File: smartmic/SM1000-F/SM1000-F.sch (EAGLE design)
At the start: 205 parts, among them CN1 HDR100-3, CN10 ST-3509, CN11 HDR100-3, CN12 HRS-A3C-16DA, CN2 JS-MU3-002, CN3 DS-0518, CN4 RJ-45, CN5 ST-3509, CN6 ST-3509, CN7 ST-3509, CN8 ST-3509, CN9 ST-3509, J1 JMP-2PIN, J2 JMP-2PIN, J3 JMP-2PIN, J4 CONN-BOOM-XH-2A, P1 TPAD50, P10 TPAD50, P11 TPAD50, P12 TPAD50, P13 TPAD50, P14 TPAD50, P16 TPAD50, P18 TPAD50, P19 TPAD50, P2 TPAD50, P20 TPAD50, P3 TPAD50, P4 TPAD50, P5 TPAD50, P6 TPAD50, P7 TPAD50, P8 TPAD50, P9 TPAD50, SW1 SW-LC2259, SW2 TS-026, SW3 SW-LC2259EENP, SW4 TS-026, SW5 TS-02B, T1 SM-LP-5001, T2 SM-LP-5001, U1 STM32F405VGT6, U2 LD3985M33R, U3 STMPS2141, U4 EMIF02-USB03F2, U5 TPS54329E, U6 LMV341, U7 LMV341, U8 LM386M-1, U9 LMV341

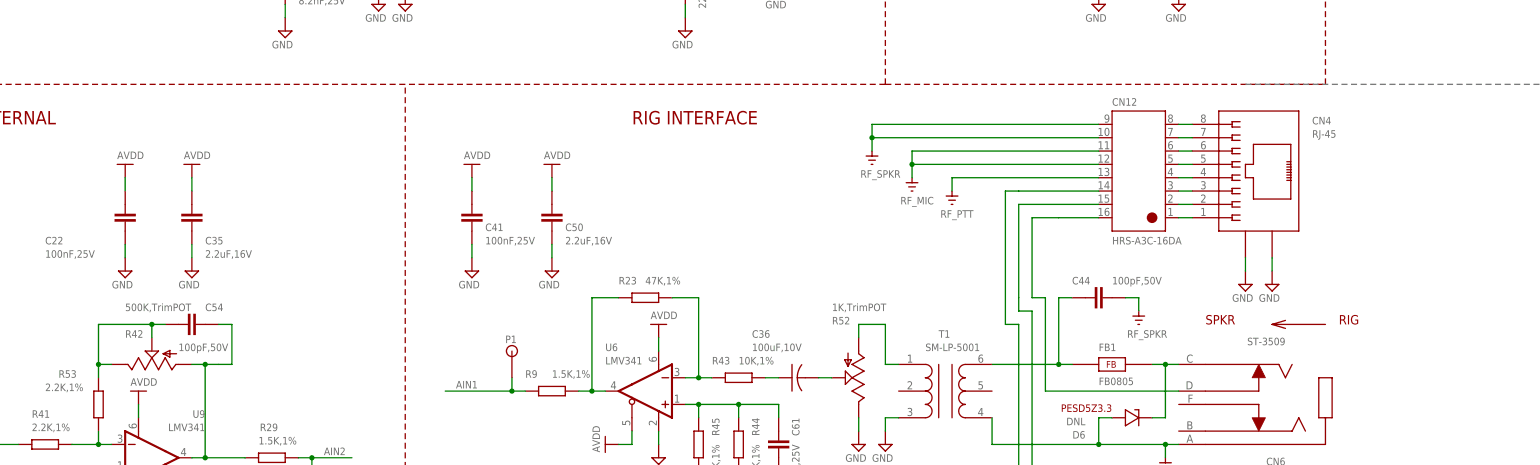
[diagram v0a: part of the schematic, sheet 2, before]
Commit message: Started implementing change-log items 34-41 RGB 09/15/15
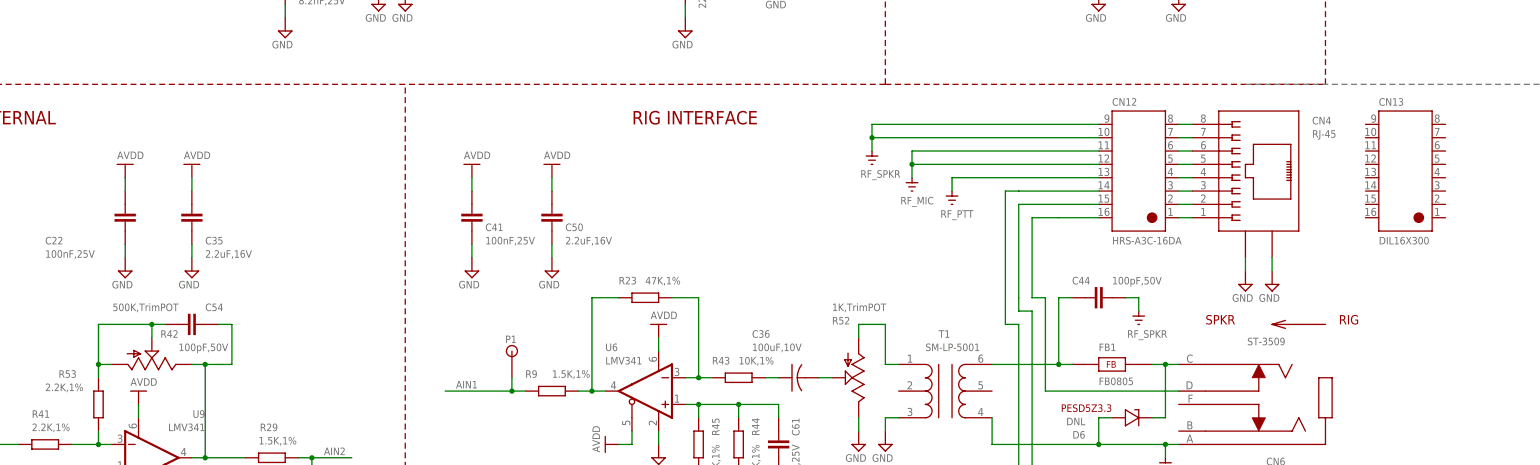
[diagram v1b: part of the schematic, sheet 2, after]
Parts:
- added CN13: DIL16X300, _RoweTel:DIL16X300
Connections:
- net N$27: now also R42.1; no longer R42.3
- net N$41: now also R42.3; no longer R42.1
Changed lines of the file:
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@@
 <part name="V143" library="A-SUPPLY2" deviceset="GND" device=""/>
 <part name="D8" library="_RoweTel" deviceset="PESD5ZX" device="" value="DNL"/>
+<part name="CN13" library="_RoweTel" deviceset="DIL16X300" device=""/>
 </parts>
 <sheets>
@@
 <attribute name="VALUE" x="106.68" y="134.62" size="1.4224" layer="96" ratio="9"/>
 </instance>
-<instance part="R42" gate="G$1" x="129.54" y="147.32" smashed="yes" rot="R90">
-<attribute name="NAME" x="124.46" y="152.4" size="1.4224" layer="95" ratio="9"/>
-<attribute name="VALUE" x="124.46" y="157.48" size="1.4224" layer="96" ratio="9"/>
+<instance part="R42" gate="G$1" x="129.54" y="147.32" smashed="yes" rot="MR90">
+<attribute name="NAME" x="134.62" y="152.4" size="1.4224" layer="95" ratio="9" rot="MR0"/>
+<attribute name="VALUE" x="134.62" y="157.48" size="1.4224" layer="96" ratio="9" rot="MR0"/>
 </instance>
 <instance part="V62" gate="GND" x="111.76" y="109.22" smashed="yes">
@@
 <attribute name="VALUE" x="45.72" y="119.38" size="1.4224" layer="96" ratio="10"/>
 </instance>
+<instance part="CN13" gate="G$1" x="368.3" y="182.88" smashed="yes">
+<attribute name="NAME" x="363.22" y="196.596" size="1.4224" layer="95" ratio="10"/>
+<attribute name="VALUE" x="363.22" y="170.18" size="1.4224" layer="96" ratio="10"/>
+</instance>
 </instances>
 <busses>
@@
 <net name="N$41" class="0">
 <segment>
-<wire x1="119.38" y1="147.32" x2="121.92" y2="147.32" width="0.1524" layer="91"/>
-<pinref part="R42" gate="G$1" pin="1"/>
-<pinref part="R42" gate="G$1" pin="2"/>
-<wire x1="129.54" y1="152.4" x2="129.54" y2="154.94" width="0.1524" layer="91"/>
 <wire x1="129.54" y1="154.94" x2="119.38" y2="154.94" width="0.1524" layer="91"/>
 <wire x1="119.38" y1="154.94" x2="119.38" y2="147.32" width="0.1524" layer="91"/>
 <pinref part="R53" gate="G$1" pin="2"/>
 <wire x1="119.38" y1="144.78" x2="119.38" y2="147.32" width="0.1524" layer="91"/>
-<junction x="119.38" y="147.32"/>
 <wire x1="129.54" y1="154.94" x2="132.08" y2="154.94" width="0.1524" layer="91"/>
-<junction x="129.54" y="154.94"/>
 <pinref part="C54" gate="G$1" pin="1"/>
+<pinref part="R42" gate="G$1" pin="3"/>
+<wire x1="121.92" y1="147.32" x2="119.38" y2="147.32" width="0.1524" layer="91"/>
+<pinref part="R42" gate="G$1" pin="2"/>
+<wire x1="129.54" y1="152.4" x2="129.54" y2="154.94" width="0.1524" layer="91"/>
+<junction x="129.54" y="154.94"/>
+<junction x="119.38" y="147.32"/>
 </segment>
 </net>
@@
 <net name="N$27" class="0">
 <segment>
-<pinref part="R42" gate="G$1" pin="3"/>
-<wire x1="137.16" y1="147.32" x2="139.7" y2="147.32" width="0.1524" layer="91"/>
 <pinref part="U9" gate="G$1" pin="OUT"/>
 <pinref part="R29" gate="G$1" pin="2"/>
@@
 <wire x1="139.7" y1="147.32" x2="139.7" y2="129.54" width="0.1524" layer="91"/>
 <junction x="139.7" y="129.54"/>
-<junction x="139.7" y="147.32"/>
 <pinref part="C54" gate="G$1" pin="2"/>
 <wire x1="142.24" y1="154.94" x2="144.78" y2="154.94" width="0.1524" layer="91"/>
 <wire x1="144.78" y1="154.94" x2="144.78" y2="147.32" width="0.1524" layer="91"/>
 <wire x1="144.78" y1="147.32" x2="142.24" y2="147.32" width="0.1524" layer="91"/>
+<pinref part="R42" gate="G$1" pin="1"/>
+<wire x1="137.16" y1="147.32" x2="139.7" y2="147.32" width="0.1524" layer="91"/>
+<junction x="139.7" y="147.32"/>
 </segment>
 </net>

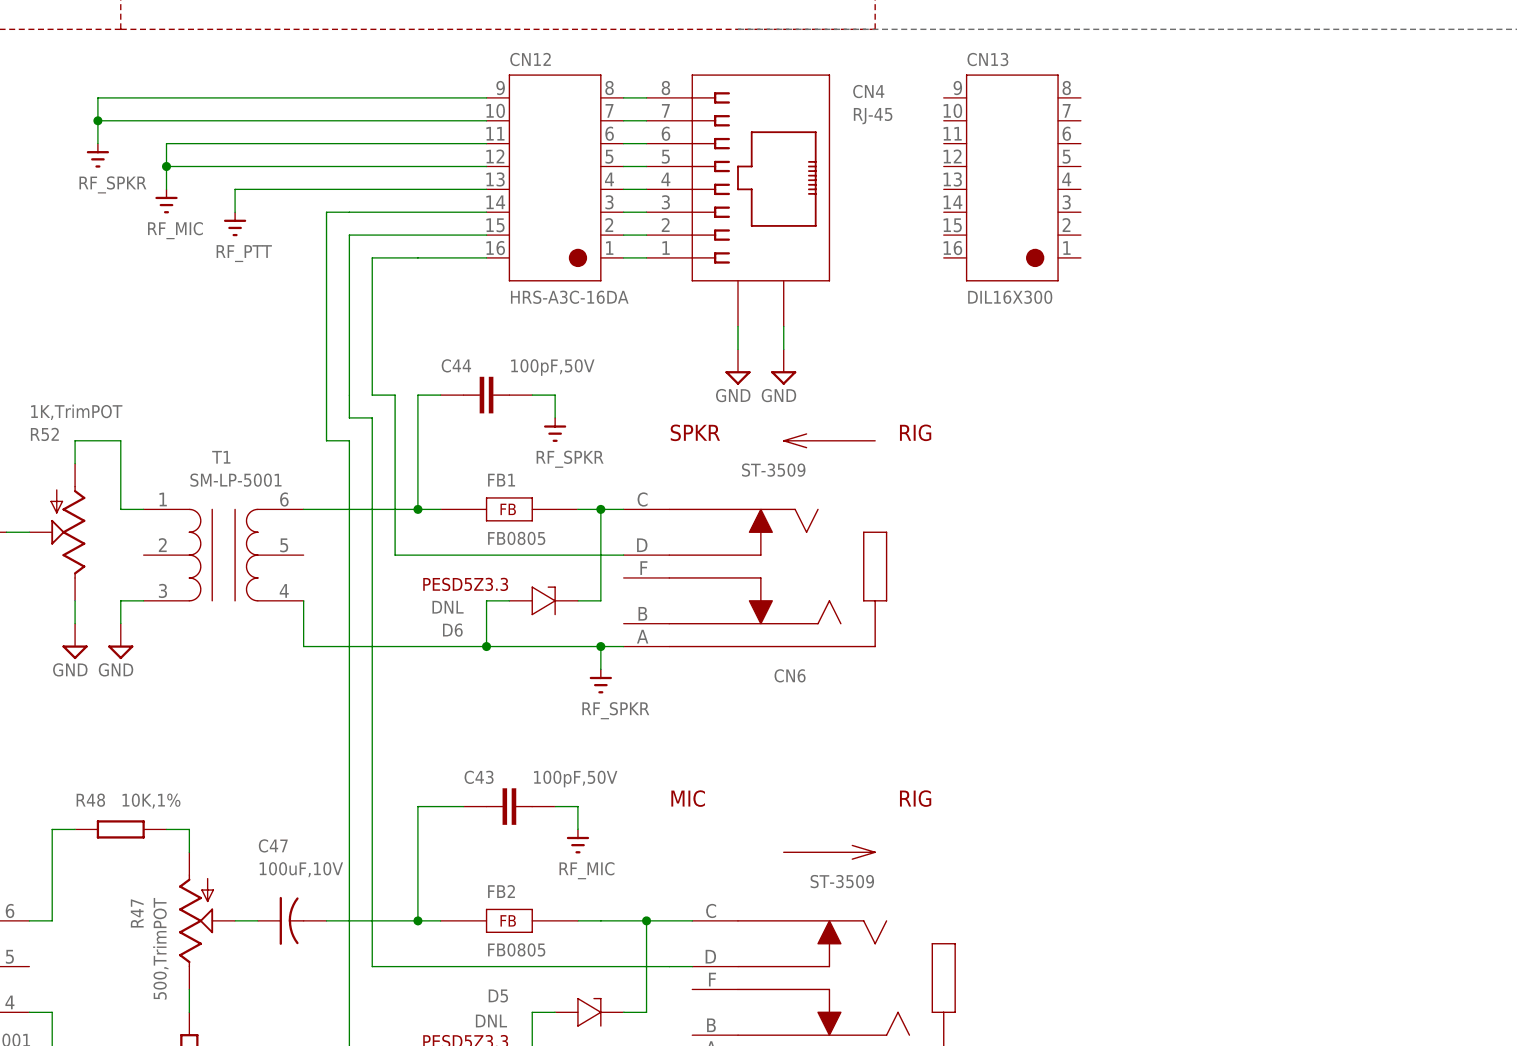
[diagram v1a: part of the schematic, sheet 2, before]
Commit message: Show Schematic changes for CN12 pin swaps.  RGB 09/16/15
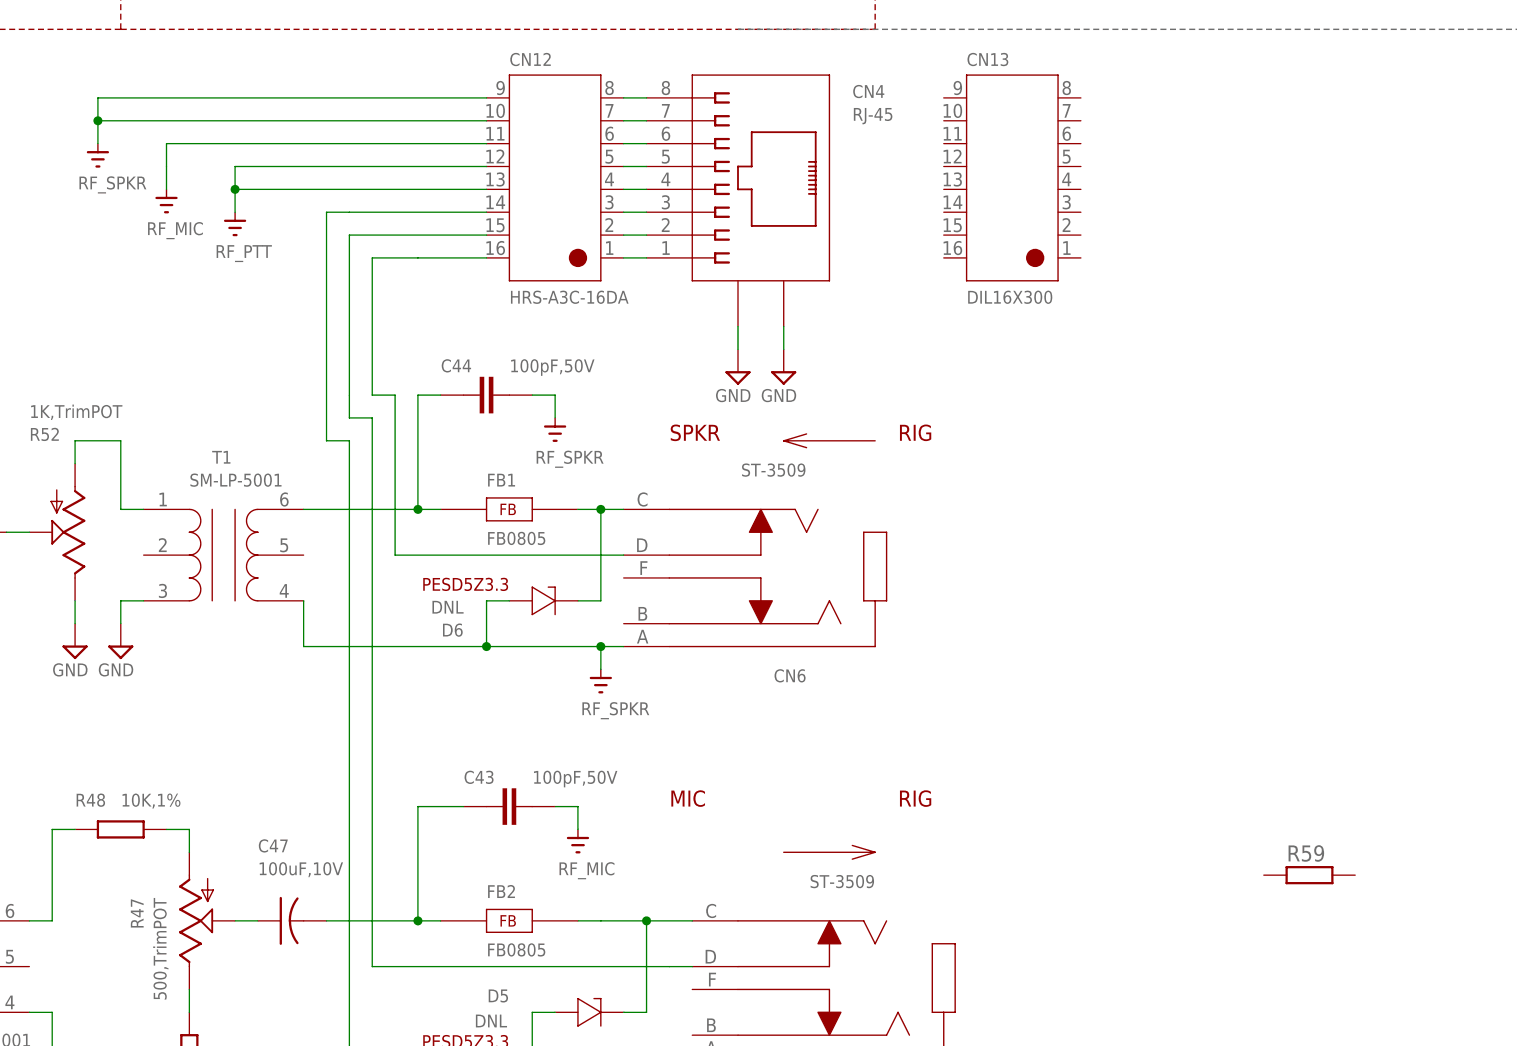
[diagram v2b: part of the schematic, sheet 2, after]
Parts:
- added R59: (no value), AA-ipc-7351-resistor:RESISTOR_1206
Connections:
- net RF_MIC: no longer CN12.12
- net RF_PTT: now also CN12.12
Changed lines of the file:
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@@
 <part name="D8" library="_RoweTel" deviceset="PESD5ZX" device="" value="DNL"/>
 <part name="CN13" library="_RoweTel" deviceset="DIL16X300" device=""/>
+<part name="R59" library="AA-ipc-7351-resistor" deviceset="RESISTOR_" device="1206"/>
 </parts>
 <sheets>
@@
 <attribute name="VALUE" x="363.22" y="170.18" size="1.4224" layer="96" ratio="10"/>
 </instance>
+<instance part="R59" gate="G$1" x="401.32" y="106.68"/>
 </instances>
 <busses>
@@
 <wire x1="274.32" y1="187.96" x2="274.32" y2="185.42" width="0.1524" layer="91"/>
 <wire x1="274.32" y1="185.42" x2="274.32" y2="182.88" width="0.1524" layer="91"/>
-<wire x1="309.88" y1="185.42" x2="274.32" y2="185.42" width="0.1524" layer="91"/>
-<junction x="274.32" y="185.42"/>
 <pinref part="V133" gate="G$1" pin="RF_MIC"/>
 <pinref part="CN12" gate="G$1" pin="11"/>
-<pinref part="CN12" gate="G$1" pin="12"/>
 </segment>
 <segment>
@@
 <pinref part="V92" gate="G$1" pin="RF_PTT"/>
 <pinref part="CN12" gate="G$1" pin="13"/>
+<pinref part="CN12" gate="G$1" pin="12"/>
+<wire x1="309.88" y1="185.42" x2="281.94" y2="185.42" width="0.1524" layer="91"/>
+<wire x1="281.94" y1="185.42" x2="281.94" y2="182.88" width="0.1524" layer="91"/>
+<junction x="281.94" y="182.88"/>
 </segment>
 </net>

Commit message: Update Schematic & board files. Add PDF of schematic for review. RGB
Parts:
- removed CN12: HRS-A3C-16DA, _RoweTel:HRS-A3C-16DA
- removed CN13: DIL16X300, _RoweTel:DIL16X300
- added CN112: DIL16X300, _RoweTel:DIL16X300
- added J5: JMP-2PIN, _Coherix:JMP-2PIN
- added P15, P17, P21: TPAD50, _Coherix:TPAD50
- added R60: 330,1%, AA-ipc-7351-resistor:RESISTOR_1206
- added R61, R62: (no value), AA-ipc-7351-resistor:RESISTOR_0603
- added SH4: SHUNT,0.1IN, _Coherix:SHUNT,0.1IN
- added U10: 24LC256-I/MS, coherix:I2C-EEPROM-256KMSOP-8
- R48: device AA-ipc-7351-resistor:RESISTOR_0402 -> AA-ipc-7351-resistor:RESISTOR_1206
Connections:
- new net N$75: J5.2, R60.1
- new net SCL3: R62.2, U10.SCL, U1A.PE10
- new net SDA3: R61.2, U10.SDA, U1A.PE9
- net APTT: now also CN112.14; no longer CN12.14
- net GND: now also P17.1, U10.A0, U10.A1, U10.A2, U10.GND, U10.WP
- net MIC: now also CN112.15; no longer CN12.15
- net N$51: now also CN112.8, P15.1; no longer CN12.8
- net N$52: now also CN112.7; no longer CN12.7
- net N$53: now also CN112.6; no longer CN12.6
- net N$54: now also CN112.5; no longer CN12.5
- net N$55: now also CN112.4; no longer CN12.4
- net N$56: now also CN112.3; no longer CN12.3
- net N$57: now also CN112.2; no longer CN12.2
- net N$58: now also CN112.1; no longer CN12.1
- net N$77: now also P21.1
- net N$78: now also R60.2
- net N$82: now also J5.1
- net RF_MIC: now also CN112.11; no longer CN12.11
- net RF_PTT: now also CN112.12, CN112.13; no longer CN12.12, CN12.13
- net RF_SPKR: now also CN112.10, CN112.9; no longer CN12.10, CN12.9
- net SPKR: now also CN112.P16; no longer CN12.P16
- net VDD: now also R61.1, R62.1, U10.VCC
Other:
- note added: "09/27/15"
- note added: "ADD EEPROM FOR PERSISTANT MEMORY."
- note added: "ADD EEPROM FOR PERSISTENT MEMORY."
- note added: "ADD PADS FOR USING RIG POWER."
- note added: "ADD R& JMPR IN PARALLEL WITH R48."
- note added: "ADDR: 0XA0"
- note added: "CHANGE GROUNDING ON CN13."
- note added: "CHANGE R48 & R60 FOR USER CHANGE."
- note added: "CN12 -> .3" DIL FOR EASIER CONFIG."
- note added: "EEPROM"
- note added: "POTS FISED FOR CW ROTATION."
- note added: "Rev E. -> Rev F CHANGES"
- note removed: "01-23-15"
- note removed: "01/13/15"
- note removed: "01/14/15"
- note removed: "01/23/15"
- note removed: "05/19/15"
- note removed: "05/20/15"
- note removed: "05/27/15"
- note removed: "06/01/15"
- note removed: "06/05/15"
- note removed: "06/26/15"
- note removed: "06/27/15"
- note removed: "11/23/14"
- note removed: "ADD D1,D3,D4,D5,D6,D7,D8 TSV"
- note removed: "ADD MISC. PARTS TO BOM"
- note removed: "CHANGE CIRCUITRY FOR CN8"
- note removed: "CHANGE CIRCUITRY TO FIX CN8 PROBLEM"
- note removed: "CHANGE LED COLORS FOR LED1 , LED4"
- note removed: "CHANGE PARTS SW1, SW3 & J4"
- note removed: "CHANGE R42,R47 & R52 TO TYPE 3361"
- note removed: "Change SW1 to MULTICOMP SPDT"
- note removed: "D"
- note removed: "DNL LED5,R17,LED8,R33"
- note removed: "E"
- note removed: "FIX TS-026 FOOTPRINT"
- note removed: "MOVE SW3,4 TO EDGE"
- note removed: "MOVE USB CONN 1MM TOWARDS EDGE"
- note removed: "NOTE: SEE PAGE 1 FOR CHANGES"
- note removed: "RELEASE REV. D TO PRODUCTION"
- note removed: "RELEASE REV. D TO PRODUCTION."
- note removed: "RELEASE TO PRODUCTION"
- note removed: "SHOW SH1 POSITION"
- note removed: "SM1000-C -> SM1000-D"
